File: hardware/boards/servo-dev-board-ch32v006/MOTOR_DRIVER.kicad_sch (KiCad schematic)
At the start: 15 parts, among them U2 DRV8212PDSGR

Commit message: updated LCSC part numbers for all symbols
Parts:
- C10, C4, C5: LCSC C307331 -> C28233
- C6: LCSC C96446 -> C440198
- C7: LCSC C96123 -> C19271225
- R5, R7: LCSC C25765 -> C4328
- R6, R8, R9: LCSC C25744 -> C17414
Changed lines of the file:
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@@
 			)
 		)
-		(property "LCSC" "C25744"
+		(property "LCSC" "C17414"
 			(at 136.906 52.832 0)
 			(effects
@@
 			)
 		)
-		(property "LCSC" "C96446"
+		(property "LCSC" "C440198"
 			(at 88.9 50.8 0)
 			(effects
@@
 			)
 		)
-		(property "LCSC" "C96123"
+		(property "LCSC" "C19271225"
 			(at 96.52 50.8 0)
 			(effects
@@
 			)
 		)
-		(property "LCSC" "C25765"
+		(property "LCSC" "C4328"
 			(at 80.518 107.188 0)
 			(effects
@@
 			)
 		)
-		(property "LCSC" "C25744"
+		(property "LCSC" "C17414"
 			(at 79.756 117.856 0)
 			(effects
@@
 			)
 		)
-		(property "LCSC" "C25765"
+		(property "LCSC" "C4328"
 			(at 103.632 107.696 0)
 			(effects
@@
 			)
 		)
-		(property "LCSC" "C307331"
+		(property "LCSC" "C28233"
 			(at 85.852 50.8 0)
 			(effects
@@
 			)
 		)
-		(property "LCSC" "C307331"
+		(property "LCSC" "C28233"
 			(at 38.1 53.34 0)
 			(effects
@@
 			)
 		)
-		(property "LCSC" "C25744"
+		(property "LCSC" "C17414"
 			(at 103.886 118.11 0)
 			(effects
@@
 			)
 		)
-		(property "LCSC" "C307331"
+		(property "LCSC" "C28233"
 			(at 189.992 52.07 0)
 			(effects

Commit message: added MFPN properties
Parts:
- C10, C4, C5: MFPN (none) -> CL21B104KCFNNNE
- C6: MFPN (none) -> GRM21BR61H106KE43L
- C7: MFPN (none) -> VT1V101M-CRE54
- FB1: MFPN (none) -> GZ2012D601TF
- R5, R7: MFPN (none) -> 0805W8F2002T5E
- R6, R8, R9: MFPN (none) -> 0805W8F1002T5E
- RS1: MFPN (none) -> 1206W4F100LT5E
- U2: MFPN (none) -> DRV8212PDSGR
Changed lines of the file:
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@@
+			)
+		)
+		(property "MFPN" "0805W8F1002T5E"
+			(at 136.906 52.832 0)
+			(effects
+				(font
+					(size 1.27 1.27)
+				)
+				(hide yes)
 			)
 		)
@@
 			)
 		)
+		(property "MFPN" "1206W4F100LT5E"
+			(at 34.29 109.22 0)
+			(effects
+				(font
+					(size 1.27 1.27)
+				)
+				(hide yes)
+			)
+		)
 		(pin "1"
 		)
@@
 		)
 		(property "LCSC" "C1017"
+			(at 34.2519 39.37 0)
+			(effects
+				(font
+					(size 1.27 1.27)
+				)
+				(hide yes)
+			)
+		)
+		(property "MFPN" "GZ2012D601TF"
 			(at 34.2519 39.37 0)
 			(effects
@@
 			)
 		)
+		(property "MFPN" "GRM21BR61H106KE43L"
+			(at 88.9 50.8 0)
+			(effects
+				(font
+					(size 1.27 1.27)
+				)
+				(hide yes)
+			)
+		)
 		(pin "1"
 		)
@@
 			)
 		)
+		(property "MFPN" "VT1V101M-CRE54"
+			(at 96.52 50.8 0)
+			(effects
+				(font
+					(size 1.27 1.27)
+				)
+				(hide yes)
+			)
+		)
 		(pin "1"
 		)
@@
 			)
 		)
+		(property "MFPN" "DRV8212PDSGR"
+			(at 162.56 54.61 0)
+			(effects
+				(font
+					(size 1.27 1.27)
+				)
+				(hide yes)
+			)
+		)
 		(property "JLC Type" "Extended"
 			(at 162.56 54.61 0)
@@
 			)
 		)
+		(property "MFPN" "0805W8F2002T5E"
+			(at 80.518 107.188 0)
+			(effects
+				(font
+					(size 1.27 1.27)
+				)
+				(hide yes)
+			)
+		)
 		(pin "1"
 		)
@@
 			)
 		)
+		(property "MFPN" "0805W8F1002T5E"
+			(at 79.756 117.856 0)
+			(effects
+				(font
+					(size 1.27 1.27)
+				)
+				(hide yes)
+			)
+		)
 		(pin "1"
 		)
@@
 			)
 		)
+		(property "MFPN" "0805W8F2002T5E"
+			(at 103.632 107.696 0)
+			(effects
+				(font
+					(size 1.27 1.27)
+				)
+				(hide yes)
+			)
+		)
 		(pin "1"
 		)
@@
 			)
 		)
+		(property "MFPN" "CL21B104KCFNNNE"
+			(at 85.852 50.8 0)
+			(effects
+				(font
+					(size 1.27 1.27)
+				)
+				(hide yes)
+			)
+		)
 		(pin "1"
 		)
@@
 			)
 		)
+		(property "MFPN" "CL21B104KCFNNNE"
+			(at 38.1 53.34 0)
+			(effects
+				(font
+					(size 1.27 1.27)
+				)
+				(hide yes)
+			)
+		)
 		(pin "1"
 		)
@@
 		)
 		(property "LCSC" "C17414"
+			(at 103.886 118.11 0)
+			(effects
+				(font
+					(size 1.27 1.27)
+				)
+				(hide yes)
+			)
+		)
+		(property "MFPN" "0805W8F1002T5E"
 			(at 103.886 118.11 0)
 			(effects
@@
 			(at 189.992 52.07 0)
 			(effects
+				(font
+					(size 1.27 1.27)
+				)
+				(hide yes)
+			)
+		)
+		(property "MFPN" "CL21B104KCFNNNE"
+			(at 189.992 52.07 0)
+			(effects

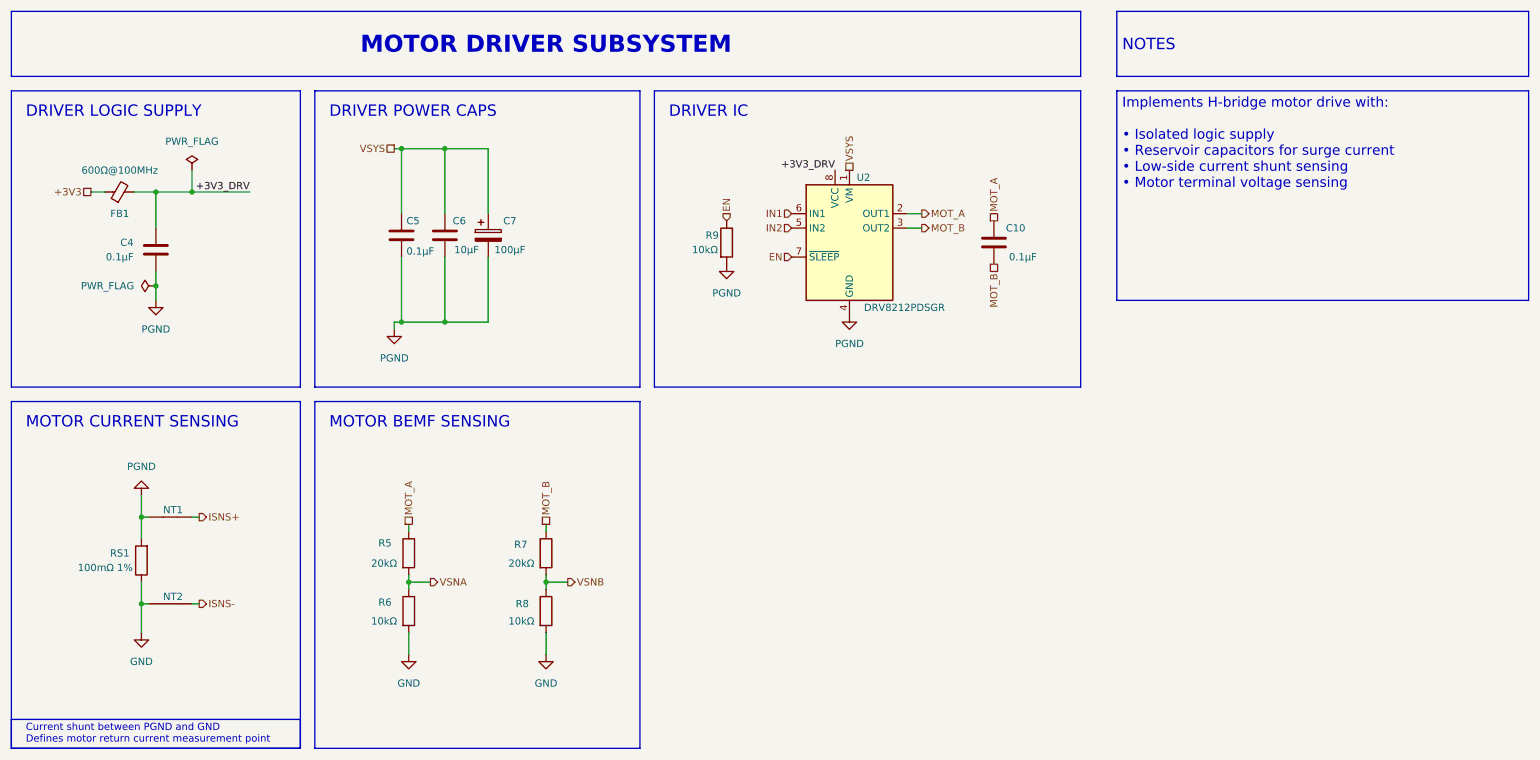
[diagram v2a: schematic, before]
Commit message: Revision V1B. Fixes:
* Fixed reversed VDD/VCC on MCU.
* Fixed TP silk screen labels on top row.
* Updated RS1 to 10mOhm/333mW.
* Updated System (green) LED resistor to 1.5kOhm to reduce brightness.
* Aligned bottom row TPs to center of board.
* Updated text on back silkscreen to reflect version / RS1 updates.
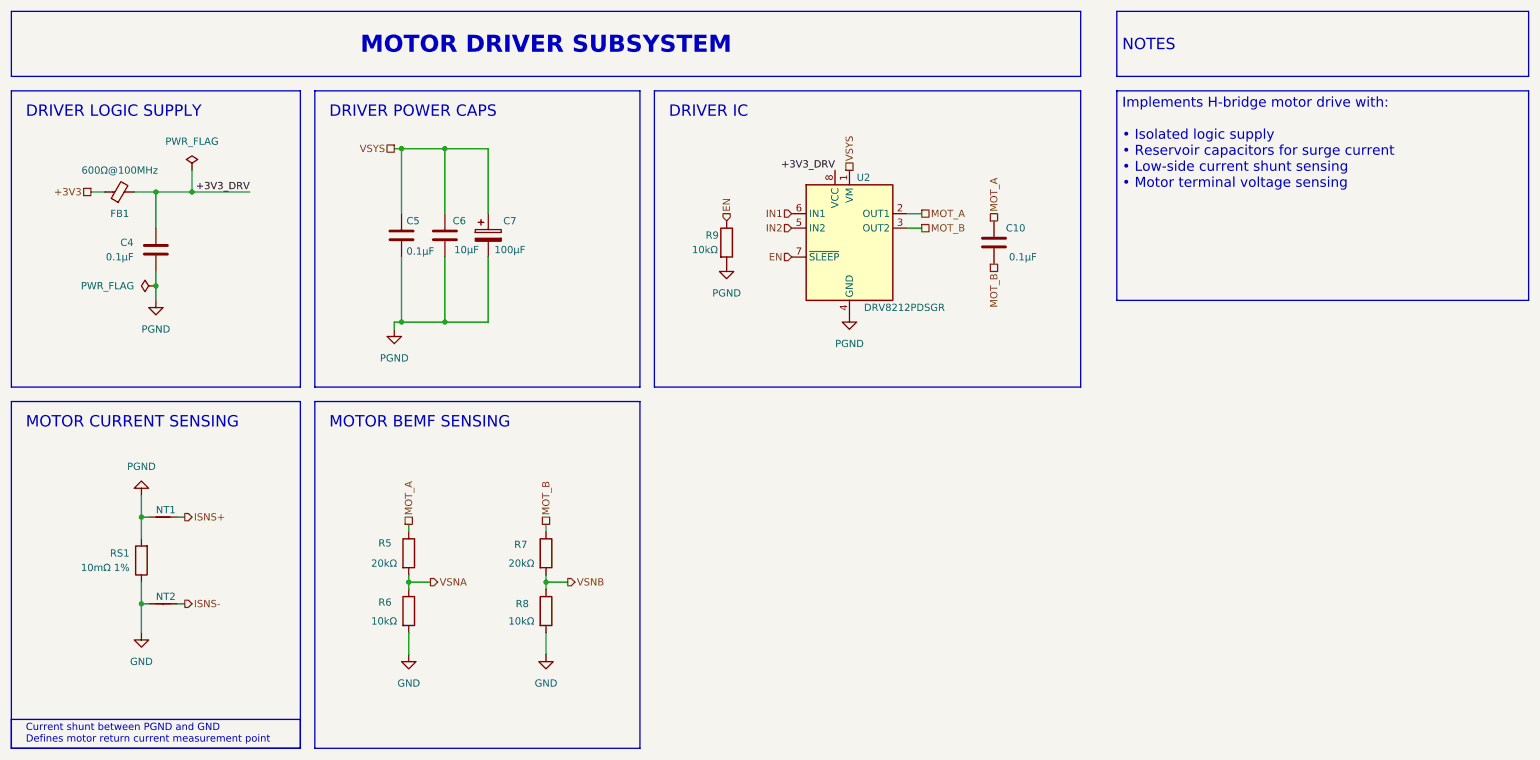
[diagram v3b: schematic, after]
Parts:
- RS1: value 100mΩ 1% -> 10mΩ 1%; LCSC C25334 -> C473031; MFPN 1206W4F100LT5E -> 1206W3F100MT5E
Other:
- moved on the sheet: NT1, NT2

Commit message: update board
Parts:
- added R10: 10kΩ, Resistor_SMD:R_0805_2012Metric_Pad1.20x1.40mm_HandSolder, symbol Device:R
- added R9: 20kΩ, Resistor_SMD:R_0805_2012Metric_Pad1.20x1.40mm_HandSolder, symbol Device:R
- renumbered C10 to C8, R9 to R11
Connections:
- net GND: now also R10.2
- net VSYS: now also R9.1
- new net VSNS: R10.1, R9.2

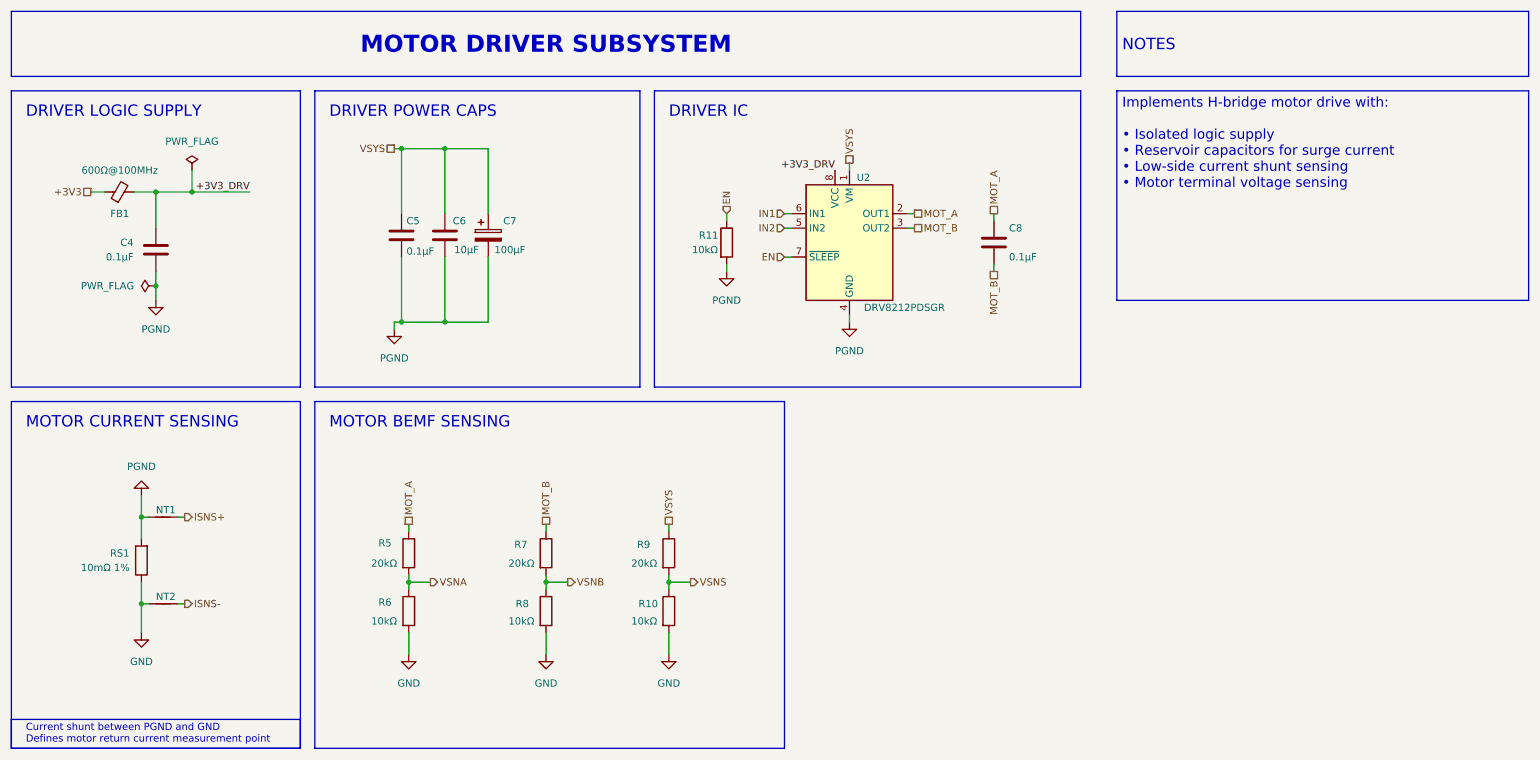
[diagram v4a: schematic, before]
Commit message: updated schematics. ERC on schematics is now passing
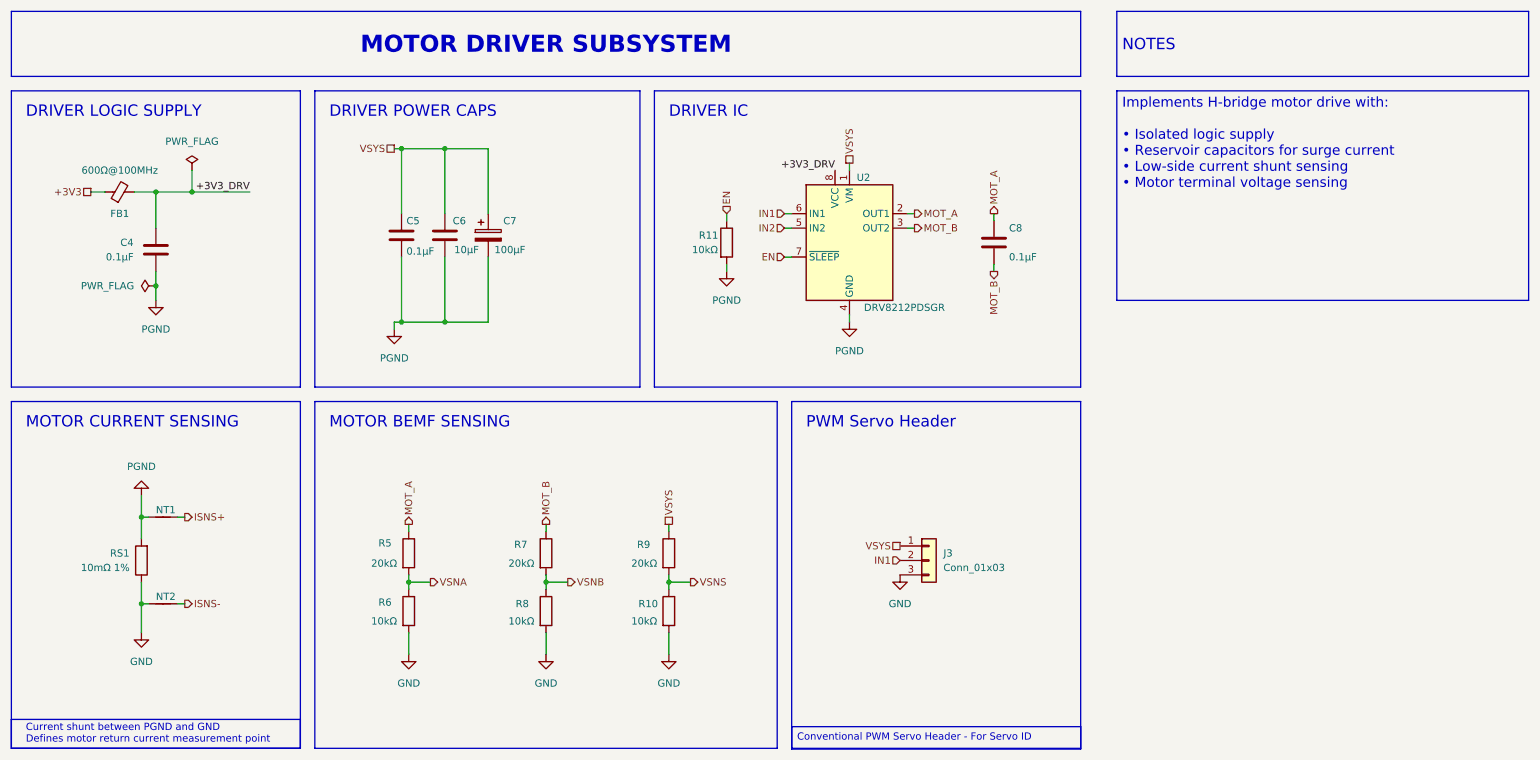
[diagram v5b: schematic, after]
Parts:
- added J3: Conn_01x03, Connector_PinHeader_2.54mm:PinHeader_1x03_P2.54mm_Vertical, symbol Connector_Generic:Conn_01x03
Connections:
- net GND: now also J3.3 (Pin_3)
- net IN1: now also J3.2 (Pin_2)
- net VSYS: now also J3.1 (Pin_1)
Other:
- note added: "PWM Servo Header"

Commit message: completed routing.
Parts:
- J3: value Conn_01x03 -> SERVO
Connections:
- net GND: now also J3.1 (Pin_1); no longer J3.3 (Pin_3)
- net IN1: now also J3.3 (Pin_3); no longer J3.2 (Pin_2)
- net VSYS: now also J3.2 (Pin_2); no longer J3.1 (Pin_1)
